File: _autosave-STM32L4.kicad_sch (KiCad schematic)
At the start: 29 parts, among them J3 Conn_01x04_Pin, SW1 SW, U17 TCAN334, U18 STM32L476RGTx, U19 MR20H40, Y1 8 MHZ Oscillator

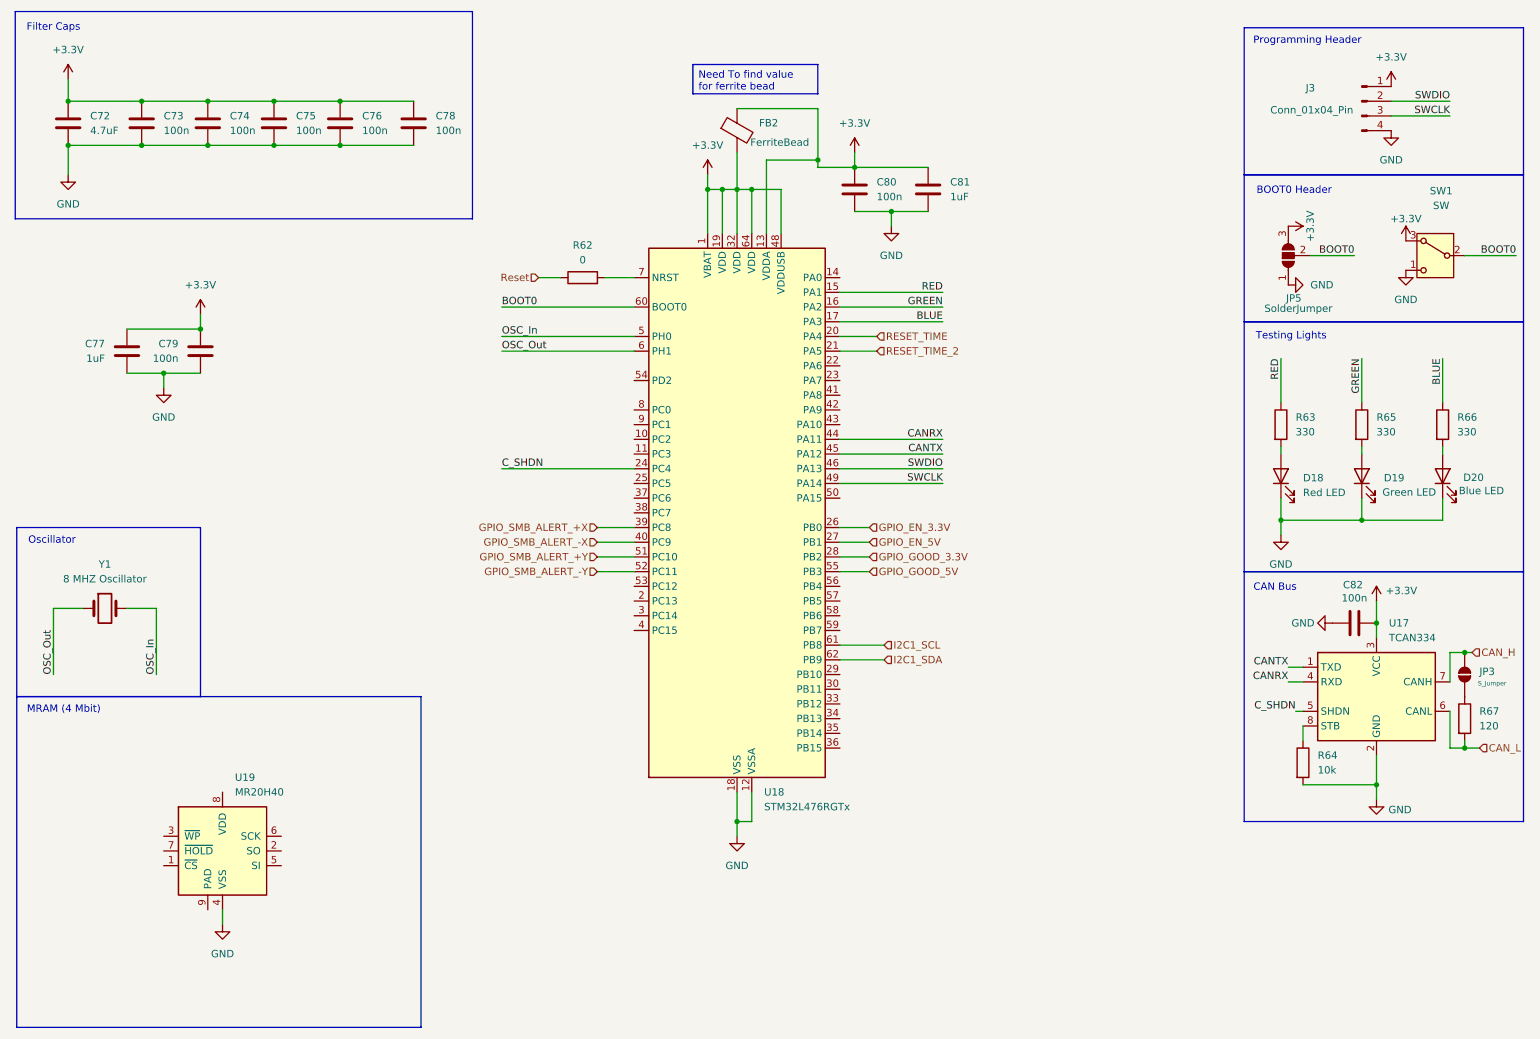
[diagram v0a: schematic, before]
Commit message: Added 3.3V and 12V lines
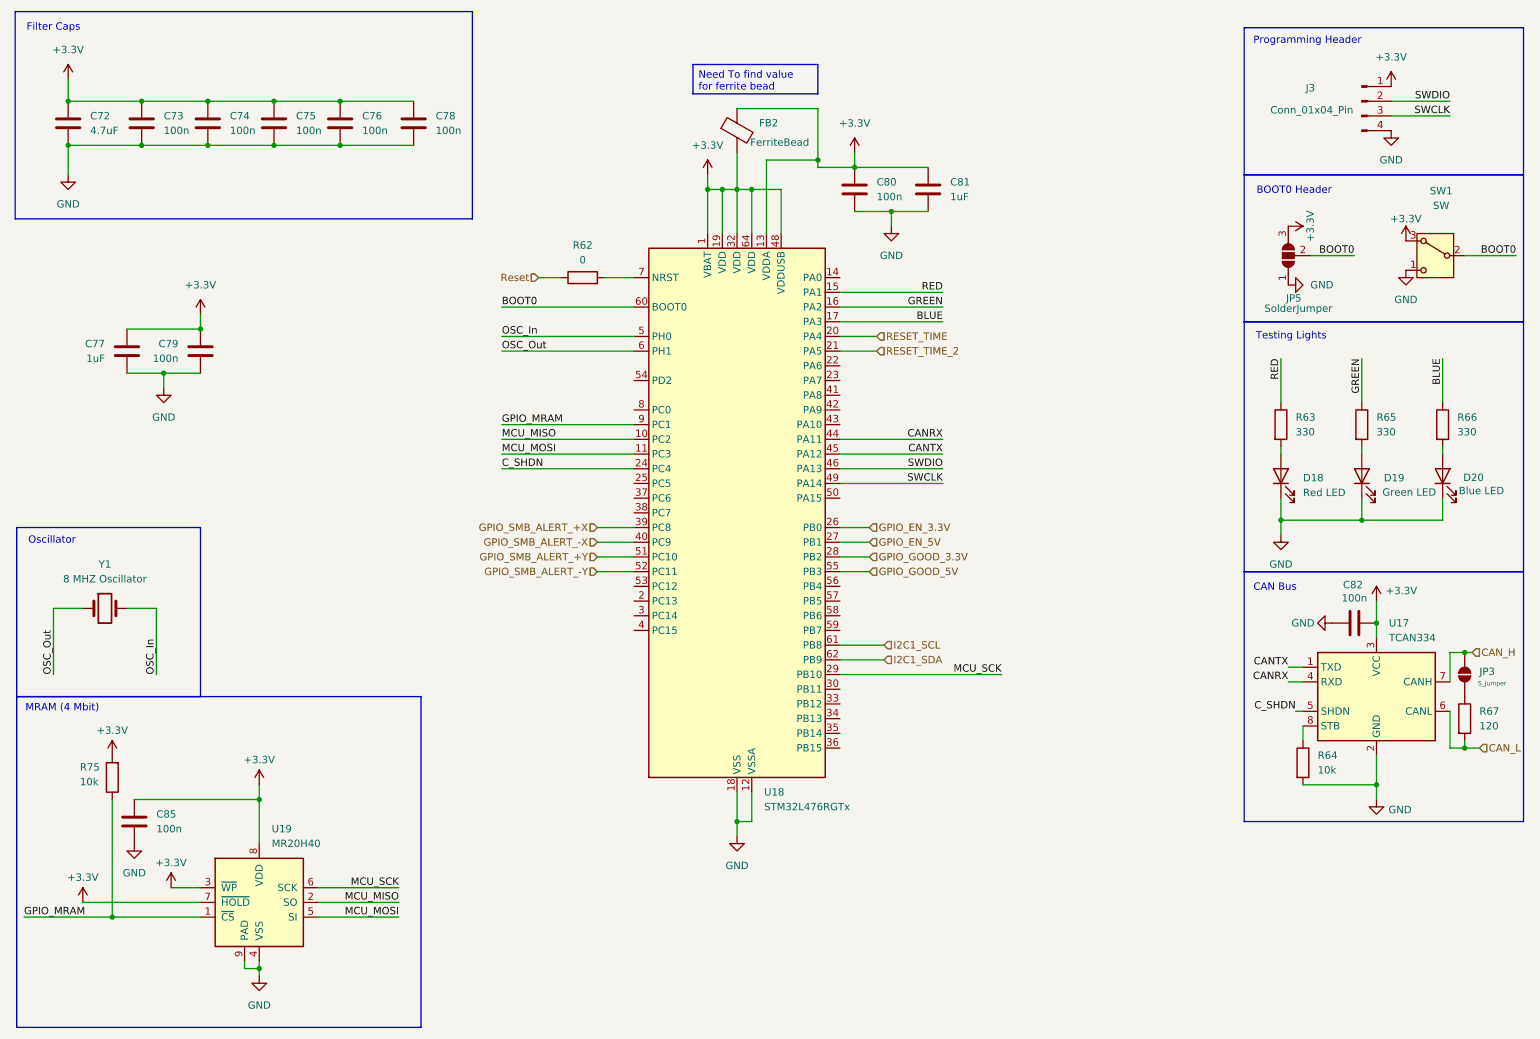
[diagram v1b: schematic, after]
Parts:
- added C85: 100n, symbol Device:C
- added R75: 10k, symbol Device:R
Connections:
- net +3.3V: now also U19.3 (~{WP}), U19.7 (~{HOLD}), U19.8 (VDD), C85.2, R75.2
- net GND: now also U19.9 (PAD), C85.1
- net MCU_MISO: now reaches U18.10 (PC2)
- net MCU_MISO: now also U19.2 (SO)
- net MCU_MOSI: now reaches U18.11 (PC3)
- net MCU_MOSI: now also U19.5 (SI)
- net MCU_SCK: now reaches U18.29 (PB10)
- net MCU_SCK: now also U19.6 (SCK)
- net GPIO_MRAM: now reaches U18.9 (PC1)
- net GPIO_MRAM: now also U19.1 (~{CS}), R75.1
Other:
- moved on the sheet: U19
